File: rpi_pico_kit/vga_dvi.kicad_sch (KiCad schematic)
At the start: 32 parts, among them J4 DB15_Female_HighDensity_Mount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, J5 HDMI_A

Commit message: added some footprints
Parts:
- J5: footprint Connector_HDMI:HDMI_A_Contact_Technology_HDMI-19APL2_Horizontal -> (none)
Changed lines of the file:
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@@
       (effects (font (size 1.27 1.27)) (justify left))
     )
-    (property "Footprint" "Connector_HDMI:HDMI_A_Contact_Technology_HDMI-19APL2_Horizontal" (id 2) (at 244.475 92.71 0)
+    (property "Footprint" "" (id 2) (at 244.475 92.71 0)
       (effects (font (size 1.27 1.27)) hide)
     )

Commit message: edited 5V I2C, added some footprints, MPNs, added HDMI footprint library
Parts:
- J5: footprint (none) -> HDMI_SS:STEWART_SS-53000-001; Manufacturer Part Number (none) -> SS-53000-001; Supplier (none) -> Digikey; Supplier Part URL (none) -> https://www.digikey.cz/en/products/detail/stewart-connector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
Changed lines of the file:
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@@
       (effects (font (size 1.27 1.27)) (justify left))
     )
-    (property "Footprint" "" (id 2) (at 244.475 92.71 0)
+    (property "Footprint" "HDMI_SS:STEWART_SS-53000-001" (id 2) (at 244.475 92.71 0)
       (effects (font (size 1.27 1.27)) hide)
     )
@@
       (effects (font (size 1.27 1.27)) hide)
     )
+    (property "Manufacturer Part Number" "SS-53000-001" (id 4) (at 243.84 92.71 0)
+      (effects (font (size 1.27 1.27)) hide)
+    )
+    (property "Supplier" "Digikey" (id 5) (at 243.84 92.71 0)
+      (effects (font (size 1.27 1.27)) hide)
+    )
+    (property "Supplier Part URL" "https://www.digikey.cz/en/products/detail/stewart-connector/SS-53000-001/10492172" (id 6) (at 243.84 92.71 0)
+      (effects (font (size 1.27 1.27)) hide)
+    )

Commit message: added MPNs for capacitors
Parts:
- C20, C43: Manufacturer Part Number (none) -> C0805C104M3RAC7800; Supplier (none) -> Digikey; Supplier Part URL (none) -> https://www.digikey.cz/en/products/detail/kemet/C0805C104M3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
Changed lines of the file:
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@@
+      (effects (font (size 1.27 1.27)) hide)
+    )
+    (property "Manufacturer Part Number" "C0805C104M3RAC7800" (id 4) (at 251.46 59.69 0)
+      (effects (font (size 1.27 1.27)) hide)
+    )
+    (property "Supplier" "Digikey" (id 5) (at 251.46 59.69 0)
+      (effects (font (size 1.27 1.27)) hide)
+    )
+    (property "Supplier Part URL" "https://www.digikey.cz/en/products/detail/kemet/C0805C104M3RAC7800/2211748" (id 6) (at 251.46 59.69 0)
       (effects (font (size 1.27 1.27)) hide)
     )
@@
       (effects (font (size 1.27 1.27)) hide)
     )
+    (property "Manufacturer Part Number" "C0805C104M3RAC7800" (id 4) (at 92.71 104.14 0)
+      (effects (font (size 1.27 1.27)) hide)
+    )
+    (property "Supplier" "Digikey" (id 5) (at 92.71 104.14 0)
+      (effects (font (size 1.27 1.27)) hide)
+    )
+    (property "Supplier Part URL" "https://www.digikey.cz/en/products/detail/kemet/C0805C104M3RAC7800/2211748" (id 6) (at 92.71 104.14 0)
+      (effects (font (size 1.27 1.27)) hide)
+    )

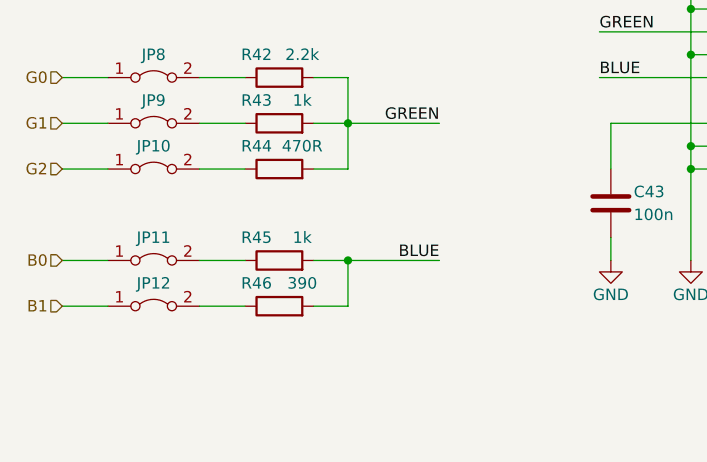
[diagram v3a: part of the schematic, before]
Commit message: added MPNs for resistors
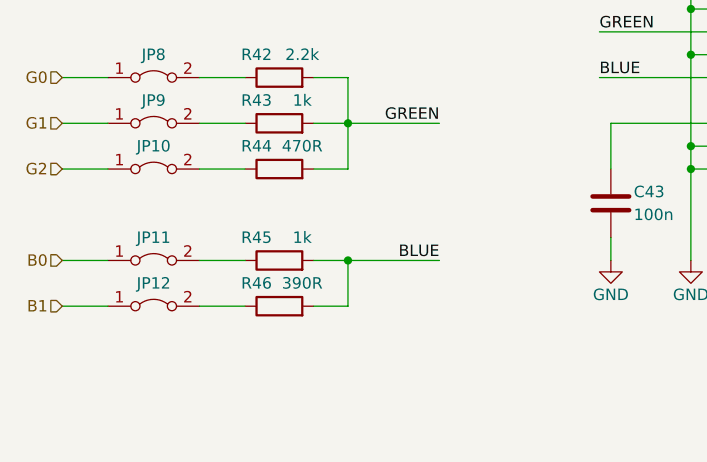
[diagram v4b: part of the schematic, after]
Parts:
- R39, R42: Manufacturer Part Number (none) -> RC0805FR-072K2L; Supplier (none) -> Digikey; Supplier Part URL (none) -> https://www.digikey.cz/en/products/detail/yageo/RC0805FR-07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
- R40, R43, R45: Manufacturer Part Number (none) -> RC0805FR-071KL; Supplier (none) -> Digikey; Supplier Part URL (none) -> https://www.digikey.cz/en/products/detail/yageo/RC0805FR-07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
- R41, R44: Manufacturer Part Number (none) -> RC0805FR-07470RL; Supplier (none) -> Digikey; Supplier Part URL (none) -> https://www.digikey.cz/en/products/detail/yageo/RC0805FR-07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
- R46: value 390 -> 390R; Manufacturer Part Number (none) -> RC0805FR-07390RL; Supplier (none) -> Digikey; Supplier Part URL (none) -> https://www.digikey.cz/en/products/detail/yageo/RC0805FR-07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
- R47, R48: Manufacturer Part Number (none) -> RC0805FR-07100RL; Supplier (none) -> Digikey; Supplier Part URL (none) -> https://www.digikey.cz/en/products/detail/yageo/RC0805FR-07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
- R49, R50, R51, R52, R53, R54, R55, R56: Manufacturer Part Number (none) -> RC0805FR-13270RL; Supplier (none) -> Digikey; Supplier Part URL (none) -> https://www.digikey.cz/en/products/detail/yageo/RC0805FR-13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
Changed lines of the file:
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@@
+      (effects (font (size 1.27 1.27)) hide)
+    )
+    (property "Manufacturer Part Number" "RC0805FR-07470RL" (id 4) (at 55.88 100.33 0)
+      (effects (font (size 1.27 1.27)) hide)
+    )
+    (property "Supplier Part URL" "https://www.digikey.cz/en/products/detail/yageo/RC0805FR-07470RL/727976" (id 5) (at 55.88 100.33 0)
+      (effects (font (size 1.27 1.27)) hide)
+    )
+    (property "Supplier" "Digikey" (id 6) (at 55.88 100.33 0)
       (effects (font (size 1.27 1.27)) hide)
     )
@@
       (effects (font (size 1.27 1.27)) hide)
     )
+    (property "Manufacturer Part Number" "RC0805FR-071KL" (id 4) (at 55.88 95.25 0)
+      (effects (font (size 1.27 1.27)) hide)
+    )
+    (property "Supplier Part URL" "https://www.digikey.cz/en/products/detail/yageo/RC0805FR-071KL/727444" (id 5) (at 55.88 95.25 0)
+      (effects (font (size 1.27 1.27)) hide)
+    )
+    (property "Supplier" "Digikey" (id 6) (at 55.88 95.25 0)
+      (effects (font (size 1.27 1.27)) hide)
+    )
     (pin "1")
     (pin "2")
@@
       (effects (font (size 1.27 1.27)) hide)
     )
+    (property "Manufacturer Part Number" "RC0805FR-07100RL" (id 4) (at 127 95.25 0)
+      (effects (font (size 1.27 1.27)) hide)
+    )
+    (property "Supplier Part URL" "https://www.digikey.cz/en/products/detail/yageo/RC0805FR-07100RL/727543" (id 5) (at 127 95.25 0)
+      (effects (font (size 1.27 1.27)) hide)
+    )
+    (property "Supplier" "Digikey" (id 6) (at 127 95.25 0)
+      (effects (font (size 1.27 1.27)) hide)
+    )
     (pin "1")
     (pin "2")
@@
       (effects (font (size 1.27 1.27)) hide)
     )
+    (property "Manufacturer Part Number" "RC0805FR-13270RL" (id 4) (at 218.44 72.39 0)
+      (effects (font (size 1.27 1.27)) hide)
+    )
+    (property "Supplier" "Digikey" (id 5) (at 218.44 72.39 0)
+      (effects (font (size 1.27 1.27)) hide)
+    )
+    (property "Supplier Part URL" "https://www.digikey.cz/en/products/detail/yageo/RC0805FR-13270RL/14286536" (id 6) (at 218.44 72.39 0)
+      (effects (font (size 1.27 1.27)) hide)
+    )
     (pin "1")
     (pin "2")
@@
       (effects (font (size 1.27 1.27)) hide)
     )
+    (property "Manufacturer Part Number" "RC0805FR-13270RL" (id 4) (at 218.44 85.09 0)
+      (effects (font (size 1.27 1.27)) hide)
+    )
+    (property "Supplier" "Digikey" (id 5) (at 218.44 85.09 0)
+      (effects (font (size 1.27 1.27)) hide)
+    )
+    (property "Supplier Part URL" "https://www.digikey.cz/en/products/detail/yageo/RC0805FR-13270RL/14286536" (id 6) (at 218.44 85.09 0)
+      (effects (font (size 1.27 1.27)) hide)
+    )
     (pin "1")
     (pin "2")
@@
     )
     (property "Datasheet" "~" (id 3) (at 55.88 69.85 0)
+      (effects (font (size 1.27 1.27)) hide)
+    )
+    (property "Manufacturer Part Number" "RC0805FR-072K2L" (id 4) (at 55.88 69.85 0)
+      (effects (font (size 1.27 1.27)) hide)
+    )
+    (property "Supplier Part URL" "https://www.digikey.cz/en/products/detail/yageo/RC0805FR-072K2L/727676" (id 5) (at 55.88 69.85 0)
+      (effects (font (size 1.27 1.27)) hide)
+    )
+    (property "Supplier" "Digikey" (id 6) (at 55.88 69.85 0)
       (effects (font (size 1.27 1.27)) hide)
     )
@@
       (effects (font (size 1.27 1.27)) hide)
     )
+    (property "Manufacturer Part Number" "RC0805FR-071KL" (id 4) (at 55.88 110.49 0)
+      (effects (font (size 1.27 1.27)) hide)
+    )
+    (property "Supplier Part URL" "https://www.digikey.cz/en/products/detail/yageo/RC0805FR-071KL/727444" (id 5) (at 55.88 110.49 0)
+      (effects (font (size 1.27 1.27)) hide)
+    )
+    (property "Supplier" "Digikey" (id 6) (at 55.88 110.49 0)
+      (effects (font (size 1.27 1.27)) hide)
+    )
     (pin "1")
     (pin "2")
@@
       (effects (font (size 1.27 1.27)) hide)
     )
+    (property "Manufacturer Part Number" "RC0805FR-07470RL" (id 4) (at 55.88 80.01 0)
+      (effects (font (size 1.27 1.27)) hide)
+    )
+    (property "Supplier Part URL" "https://www.digikey.cz/en/products/detail/yageo/RC0805FR-07470RL/727976" (id 5) (at 55.88 80.01 0)
+      (effects (font (size 1.27 1.27)) hide)
+    )
+    (property "Supplier" "Digikey" (id 6) (at 55.88 80.01 0)
+      (effects (font (size 1.27 1.27)) hide)
+    )
     (pin "1")
     (pin "2")
@@
     )
     (property "Datasheet" "~" (id 3) (at 218.44 74.93 0)
+      (effects (font (size 1.27 1.27)) hide)
+    )
+    (property "Manufacturer Part Number" "RC0805FR-13270RL" (id 4) (at 218.44 74.93 0)
+      (effects (font (size 1.27 1.27)) hide)
+    )
+    (property "Supplier" "Digikey" (id 5) (at 218.44 74.93 0)
+      (effects (font (size 1.27 1.27)) hide)
+    )
+    (property "Supplier Part URL" "https://www.digikey.cz/en/products/detail/yageo/RC0805FR-13270RL/14286536" (id 6) (at 218.44 74.93 0)
       (effects (font (size 1.27 1.27)) hide)
     )
@@
       (effects (font (size 1.27 1.27)) hide)
     )
+    (property "Manufacturer Part Number" "RC0805FR-13270RL" (id 4) (at 218.44 77.47 0)
+      (effects (font (size 1.27 1.27)) hide)
+    )
+    (property "Supplier" "Digikey" (id 5) (at 218.44 77.47 0)
+      (effects (font (size 1.27 1.27)) hide)
+    )
+    (property "Supplier Part URL" "https://www.digikey.cz/en/products/detail/yageo/RC0805FR-13270RL/14286536" (id 6) (at 218.44 77.47 0)
+      (effects (font (size 1.27 1.27)) hide)
+    )
     (pin "1")
     (pin "2")
@@
       (effects (font (size 1.27 1.27)) hide)
     )
+    (property "Manufacturer Part Number" "RC0805FR-13270RL" (id 4) (at 218.44 80.01 0)
+      (effects (font (size 1.27 1.27)) hide)
+    )
+    (property "Supplier" "Digikey" (id 5) (at 218.44 80.01 0)
+      (effects (font (size 1.27 1.27)) hide)
+    )
+    (property "Supplier Part URL" "https://www.digikey.cz/en/products/detail/yageo/RC0805FR-13270RL/14286536" (id 6) (at 218.44 80.01 0)
+      (effects (font (size 1.27 1.27)) hide)
+    )
     (pin "1")
     (pin "2")
@@
       (effects (font (size 1.27 1.27)) hide)
     )
+    (property "Manufacturer Part Number" "RC0805FR-072K2L" (id 4) (at 55.88 90.17 0)
+      (effects (font (size 1.27 1.27)) hide)
+    )
+    (property "Supplier Part URL" "https://www.digikey.cz/en/products/detail/yageo/RC0805FR-072K2L/727676" (id 5) (at 55.88 90.17 0)
+      (effects (font (size 1.27 1.27)) hide)
+    )
+    (property "Supplier" "Digikey" (id 6) (at 55.88 90.17 0)
+      (effects (font (size 1.27 1.27)) hide)
+    )
     (pin "1")
     (pin "2")
@@
     )
     (property "Datasheet" "~" (id 3) (at 55.88 74.93 0)
+      (effects (font (size 1.27 1.27)) hide)
+    )
+    (property "Manufacturer Part Number" "RC0805FR-071KL" (id 4) (at 55.88 74.93 0)
+      (effects (font (size 1.27 1.27)) hide)
+    )
+    (property "Supplier Part URL" "https://www.digikey.cz/en/products/detail/yageo/RC0805FR-071KL/727444" (id 5) (at 55.88 74.93 0)
+      (effects (font (size 1.27 1.27)) hide)
+    )
+    (property "Supplier" "Digikey" (id 6) (at 55.88 74.93 0)
       (effects (font (size 1.27 1.27)) hide)
     )
@@
       (effects (font (size 1.27 1.27)) hide)
     )
+    (property "Manufacturer Part Number" "RC0805FR-07100RL" (id 4) (at 127 90.17 0)
+      (effects (font (size 1.27 1.27)) hide)
+    )
+    (property "Supplier Part URL" "https://www.digikey.cz/en/products/detail/yageo/RC0805FR-07100RL/727543" (id 5) (at 127 90.17 0)
+      (effects (font (size 1.27 1.27)) hide)
+    )
+    (property "Supplier" "Digikey" (id 6) (at 127 90.17 0)
+      (effects (font (size 1.27 1.27)) hide)
+    )
     (pin "1")
     (pin "2")
@@
       (effects (font (size 1.27 1.27)))
     )
-    (property "Value" "390" (id 1) (at 58.42 113.03 90)
+    (property "Value" "390R" (id 1) (at 58.42 113.03 90)
       (effects (font (size 1.27 1.27)))
     )
@@
       (effects (font (size 1.27 1.27)) hide)
     )
+    (property "Manufacturer Part Number" "RC0805FR-07390RL" (id 4) (at 55.88 115.57 0)
+      (effects (font (size 1.27 1.27)) hide)
+    )
+    (property "Supplier" "Digikey" (id 5) (at 55.88 115.57 0)
+      (effects (font (size 1.27 1.27)) hide)
+    )
+    (property "Supplier Part URL" "https://www.digikey.cz/en/products/detail/yageo/RC0805FR-07390RL/727902" (id 6) (at 55.88 115.57 0)
+      (effects (font (size 1.27 1.27)) hide)
+    )
     (pin "1")
     (pin "2")
@@
       (effects (font (size 1.27 1.27)) hide)
     )
+    (property "Manufacturer Part Number" "RC0805FR-13270RL" (id 4) (at 218.44 87.63 0)
+      (effects (font (size 1.27 1.27)) hide)
+    )
+    (property "Supplier" "Digikey" (id 5) (at 218.44 87.63 0)
+      (effects (font (size 1.27 1.27)) hide)
+    )
+    (property "Supplier Part URL" "https://www.digikey.cz/en/products/detail/yageo/RC0805FR-13270RL/14286536" (id 6) (at 218.44 87.63 0)
+      (effects (font (size 1.27 1.27)) hide)
+    )
     (pin "1")
     (pin "2")
@@
       (effects (font (size 1.27 1.27)) hide)
     )
+    (property "Manufacturer Part Number" "RC0805FR-13270RL" (id 4) (at 218.44 82.55 0)
+      (effects (font (size 1.27 1.27)) hide)
+    )
+    (property "Supplier" "Digikey" (id 5) (at 218.44 82.55 0)
+      (effects (font (size 1.27 1.27)) hide)
+    )
+    (property "Supplier Part URL" "https://www.digikey.cz/en/products/detail/yageo/RC0805FR-13270RL/14286536" (id 6) (at 218.44 82.55 0)
+      (effects (font (size 1.27 1.27)) hide)
+    )
     (pin "1")
     (pin "2")
@@
       (effects (font (size 1.27 1.27)) hide)
     )
+    (property "Manufacturer Part Number" "RC0805FR-13270RL" (id 4) (at 218.44 90.17 0)
+      (effects (font (size 1.27 1.27)) hide)
+    )
+    (property "Supplier" "Digikey" (id 5) (at 218.44 90.17 0)
+      (effects (font (size 1.27 1.27)) hide)
+    )
+    (property "Supplier Part URL" "https://www.digikey.cz/en/products/detail/yageo/RC0805FR-13270RL/14286536" (id 6) (at 218.44 90.17 0)
+      (effects (font (size 1.27 1.27)) hide)
+    )

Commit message: little changes
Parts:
- JP10, JP11, JP12, JP13, JP14, JP3, JP6, JP7, JP8, JP9: footprint TestPoint:TestPoint_2Pads_Pitch2.54mm_Drill0.8mm -> Connector_PinHeader_2.54mm:PinHeader_1x02_P2.54mm_Vertical
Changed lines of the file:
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@@
       (effects (font (size 1.27 1.27)) hide)
     )
-    (property "Footprint" "TestPoint:TestPoint_2Pads_Pitch2.54mm_Drill0.8mm" (id 2) (at 140.97 90.17 0)
+    (property "Footprint" "Connector_PinHeader_2.54mm:PinHeader_1x02_P2.54mm_Vertical" (id 2) (at 140.97 90.17 0)
       (effects (font (size 1.27 1.27)) hide)
     )
@@
       (effects (font (size 1.27 1.27)) hide)
     )
-    (property "Footprint" "TestPoint:TestPoint_2Pads_Pitch2.54mm_Drill0.8mm" (id 2) (at 41.91 115.57 0)
+    (property "Footprint" "Connector_PinHeader_2.54mm:PinHeader_1x02_P2.54mm_Vertical" (id 2) (at 41.91 115.57 0)
       (effects (font (size 1.27 1.27)) hide)
     )
@@
       (effects (font (size 1.27 1.27)) hide)
     )
-    (property "Footprint" "TestPoint:TestPoint_2Pads_Pitch2.54mm_Drill0.8mm" (id 2) (at 41.91 95.25 0)
+    (property "Footprint" "Connector_PinHeader_2.54mm:PinHeader_1x02_P2.54mm_Vertical" (id 2) (at 41.91 95.25 0)
       (effects (font (size 1.27 1.27)) hide)
     )
@@
       (effects (font (size 1.27 1.27)) hide)
     )
-    (property "Footprint" "TestPoint:TestPoint_2Pads_Pitch2.54mm_Drill0.8mm" (id 2) (at 41.91 100.33 0)
+    (property "Footprint" "Connector_PinHeader_2.54mm:PinHeader_1x02_P2.54mm_Vertical" (id 2) (at 41.91 100.33 0)
       (effects (font (size 1.27 1.27)) hide)
     )
@@
       (effects (font (size 1.27 1.27)) hide)
     )
-    (property "Footprint" "TestPoint:TestPoint_2Pads_Pitch2.54mm_Drill0.8mm" (id 2) (at 41.91 80.01 0)
+    (property "Footprint" "Connector_PinHeader_2.54mm:PinHeader_1x02_P2.54mm_Vertical" (id 2) (at 41.91 80.01 0)
       (effects (font (size 1.27 1.27)) hide)
     )
@@
       (effects (font (size 1.27 1.27)) hide)
     )
-    (property "Footprint" "TestPoint:TestPoint_2Pads_Pitch2.54mm_Drill0.8mm" (id 2) (at 41.91 69.85 0)
+    (property "Footprint" "Connector_PinHeader_2.54mm:PinHeader_1x02_P2.54mm_Vertical" (id 2) (at 41.91 69.85 0)
       (effects (font (size 1.27 1.27)) hide)
     )
@@
       (effects (font (size 1.27 1.27)) hide)
     )
-    (property "Footprint" "TestPoint:TestPoint_2Pads_Pitch2.54mm_Drill0.8mm" (id 2) (at 140.97 95.25 0)
+    (property "Footprint" "Connector_PinHeader_2.54mm:PinHeader_1x02_P2.54mm_Vertical" (id 2) (at 140.97 95.25 0)
       (effects (font (size 1.27 1.27)) hide)
     )
@@
       (effects (font (size 1.27 1.27)) hide)
     )
-    (property "Footprint" "TestPoint:TestPoint_2Pads_Pitch2.54mm_Drill0.8mm" (id 2) (at 41.91 74.93 0)
+    (property "Footprint" "Connector_PinHeader_2.54mm:PinHeader_1x02_P2.54mm_Vertical" (id 2) (at 41.91 74.93 0)
       (effects (font (size 1.27 1.27)) hide)
     )
@@
       (effects (font (size 1.27 1.27)) hide)
     )
-    (property "Footprint" "TestPoint:TestPoint_2Pads_Pitch2.54mm_Drill0.8mm" (id 2) (at 41.91 110.49 0)
+    (property "Footprint" "Connector_PinHeader_2.54mm:PinHeader_1x02_P2.54mm_Vertical" (id 2) (at 41.91 110.49 0)
       (effects (font (size 1.27 1.27)) hide)
     )
@@
       (effects (font (size 1.27 1.27)) hide)
     )
-    (property "Footprint" "TestPoint:TestPoint_2Pads_Pitch2.54mm_Drill0.8mm" (id 2) (at 41.91 90.17 0)
-      (effects (font (size 1.27 1.27)) hide)
-    )
+    (property "Footprint" "Connector_PinHeader_2.54mm:PinHeader_1x02_P2.54mm_Vertical" (id 2) (at 41.91 90.17 0)
+      (effects (font (size 1.27 1.27)) hide)
+    )

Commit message: added another MPNs, edited color of LEDs
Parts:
- JP10, JP11, JP12, JP13, JP14, JP3, JP6, JP7, JP8, JP9: Manufacturer Part Number (none) -> PinHeader_1x02
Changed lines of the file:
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@@
+      (effects (font (size 1.27 1.27)) hide)
+    )
+    (property "Manufacturer Part Number" "PinHeader_1x02" (id 4) (at 140.97 90.17 0)
       (effects (font (size 1.27 1.27)) hide)
     )
@@
       (effects (font (size 1.27 1.27)) hide)
     )
-    (property "Datasheet" " ~" (id 3) (at 88.9 80.01 0)
+    (property "Datasheet" "~" (id 3) (at 88.9 80.01 0)
       (effects (font (size 1.27 1.27)) hide)
     )
@@
       (effects (font (size 1.27 1.27)) hide)
     )
+    (property "Manufacturer Part Number" "PinHeader_1x02" (id 4) (at 41.91 115.57 0)
+      (effects (font (size 1.27 1.27)) hide)
+    )
     (pin "1")
     (pin "2")
@@
     )
     (property "Datasheet" "~" (id 3) (at 41.91 95.25 0)
+      (effects (font (size 1.27 1.27)) hide)
+    )
+    (property "Manufacturer Part Number" "PinHeader_1x02" (id 4) (at 41.91 95.25 0)
       (effects (font (size 1.27 1.27)) hide)
     )
@@
       (effects (font (size 1.27 1.27)) hide)
     )
+    (property "Manufacturer Part Number" "PinHeader_1x02" (id 4) (at 41.91 100.33 0)
+      (effects (font (size 1.27 1.27)) hide)
+    )
     (pin "1")
     (pin "2")
@@
       (effects (font (size 1.27 1.27)) hide)
     )
+    (property "Manufacturer Part Number" "PinHeader_1x02" (id 4) (at 41.91 80.01 0)
+      (effects (font (size 1.27 1.27)) hide)
+    )
     (pin "1")
     (pin "2")
@@
     )
     (property "Datasheet" "~" (id 3) (at 41.91 69.85 0)
+      (effects (font (size 1.27 1.27)) hide)
+    )
+    (property "Manufacturer Part Number" "PinHeader_1x02" (id 4) (at 41.91 69.85 0)
       (effects (font (size 1.27 1.27)) hide)
     )
@@
       (effects (font (size 1.27 1.27)) hide)
     )
+    (property "Manufacturer Part Number" "PinHeader_1x02" (id 4) (at 140.97 95.25 0)
+      (effects (font (size 1.27 1.27)) hide)
+    )
     (pin "1")
     (pin "2")
@@
       (effects (font (size 1.27 1.27)) hide)
     )
+    (property "Manufacturer Part Number" "PinHeader_1x02" (id 4) (at 41.91 74.93 0)
+      (effects (font (size 1.27 1.27)) hide)
+    )
     (pin "1")
     (pin "2")
@@
       (effects (font (size 1.27 1.27)) hide)
     )
+    (property "Manufacturer Part Number" "PinHeader_1x02" (id 4) (at 41.91 110.49 0)
+      (effects (font (size 1.27 1.27)) hide)
+    )
     (pin "1")
     (pin "2")
@@
       (effects (font (size 1.27 1.27)) hide)
     )
+    (property "Manufacturer Part Number" "PinHeader_1x02" (id 4) (at 41.91 90.17 0)
+      (effects (font (size 1.27 1.27)) hide)
+    )
